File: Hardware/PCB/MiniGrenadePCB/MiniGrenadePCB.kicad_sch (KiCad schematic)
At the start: 3 parts, among them U1 DF-Player_mini, U2 WeMos_D1_mini

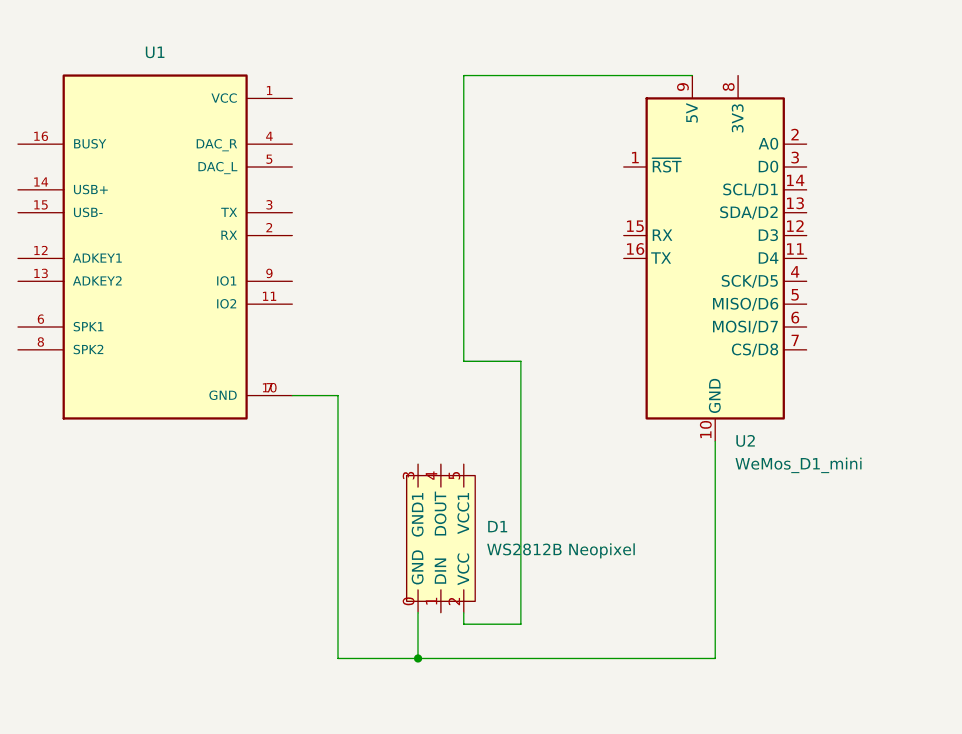
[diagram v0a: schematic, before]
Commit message: Corrected PCB Oopsie+ began small grenade PCB
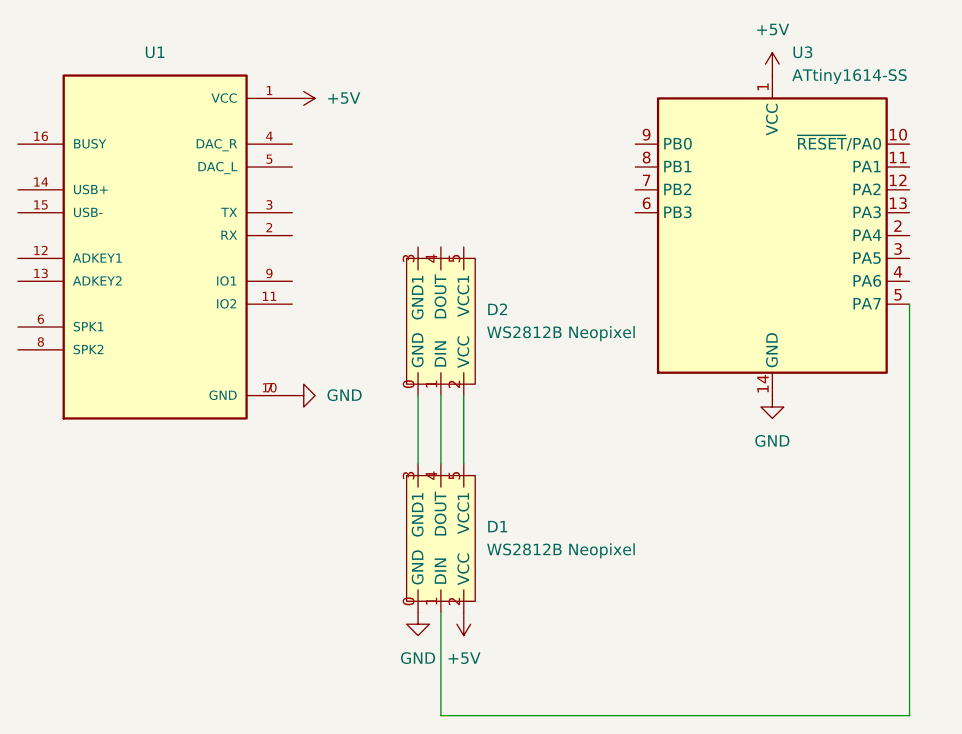
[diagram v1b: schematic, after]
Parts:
- removed U2: WeMos_D1_mini, Module:WEMOS_D1_mini_light, symbol MCU_Module:WeMos_D1_mini
- added D2: WS2812B Neopixel, Grenade_Stuff:NeoPixel_strip, symbol GrenadeStuff:NeoPixelStrip
- added U3: ATtiny1614-SS, Package_SO:SOIC-14_3.9x8.7mm_P1.27mm, symbol MCU_Microchip_ATtiny:ATtiny1614-SS
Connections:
- net GND: now reaches D1.0 (GND), U1.10 (GND), U1.7 (GND)
- net GND: now also U3.14 (GND)
- net at D1.1 (DIN): now also U3.5 (PA7)
- net +5V: now reaches D1.2 (VCC)
- net +5V: now also U1.1 (VCC), U3.1 (VCC)
- net at D1.3 (GND1): now also D2.0 (GND)
- net at D1.4 (DOUT): now also D2.1 (DIN)
- net at D1.5 (VCC1): now also D2.2 (VCC)
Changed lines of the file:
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@@
 (kicad_sch (version 20230121) (generator eeschema)
   (paper "A4")
-  (junction (at 165.1 138.43) (diameter 0) (color 0 0 0 0)
-  )
-  (wire (pts (xy 198.12 138.43) (xy 198.12 114.3))
-    (stroke (width 0) (type default))
-  )
-  (wire (pts (xy 170.18 73.66) (xy 170.18 105.41))
-    (stroke (width 0) (type default))
-  )
-  (wire (pts (xy 176.53 105.41) (xy 176.53 134.62))
-    (stroke (width 0) (type default))
-  )
-  (wire (pts (xy 170.18 105.41) (xy 176.53 105.41))
-    (stroke (width 0) (type default))
-  )
-  (wire (pts (xy 170.18 73.66) (xy 195.58 73.66))
-    (stroke (width 0) (type default))
-  )
-  (wire (pts (xy 165.1 138.43) (xy 165.1 133.35))
-    (stroke (width 0) (type default))
-  )
-  (wire (pts (xy 151.13 109.22) (xy 156.21 109.22))
-    (stroke (width 0) (type default))
-  )
-  (wire (pts (xy 170.18 134.62) (xy 170.18 133.35))
-    (stroke (width 0) (type default))
-  )
-  (wire (pts (xy 156.21 109.22) (xy 156.21 138.43))
-    (stroke (width 0) (type default))
-  )
-  (wire (pts (xy 165.1 138.43) (xy 198.12 138.43))
-    (stroke (width 0) (type default))
-  )
-  (wire (pts (xy 156.21 138.43) (xy 165.1 138.43))
-    (stroke (width 0) (type default))
-  )
-  (wire (pts (xy 176.53 134.62) (xy 170.18 134.62))
+  (wire (pts (xy 165.1 109.22) (xy 165.1 116.84))
+    (stroke (width 0) (type default))
+  )
+  (wire (pts (xy 170.18 109.22) (xy 170.18 116.84))
+    (stroke (width 0) (type default))
+  )
+  (wire (pts (xy 167.64 109.22) (xy 167.64 116.84))
+    (stroke (width 0) (type default))
+  )
+  (wire (pts (xy 167.64 133.35) (xy 167.64 144.78))
+    (stroke (width 0) (type default))
+  )
+  (wire (pts (xy 219.71 99.06) (xy 219.71 144.78))
+    (stroke (width 0) (type default))
+  )
+  (wire (pts (xy 167.64 144.78) (xy 219.71 144.78))
     (stroke (width 0) (type default))
   )
@@
     )
   )
-  (symbol (lib_id "MCU_Module:WeMos_D1_mini") (at 198.12 93.98 0) (unit 1)
-    (in_bom yes) (on_board yes) (dnp no) (fields_autoplaced)
-    (property "Reference" "U2" (at 200.3141 114.3 0)
-      (effects (font (size 1.27 1.27)) (justify left))
-    )
-    (property "Value" "WeMos_D1_mini" (at 200.3141 116.84 0)
-      (effects (font (size 1.27 1.27)) (justify left))
-    )
-    (property "Footprint" "Module:WEMOS_D1_mini_light" (at 198.12 123.19 0)
-      (effects (font (size 1.27 1.27)) hide)
-    )
-    (property "Datasheet" "https://wiki.wemos.cc/products:d1:d1_mini#documentation" (at 151.13 123.19 0)
-      (effects (font (size 1.27 1.27)) hide)
-    )
-    (pin "7")
-    (pin "13")
-    (pin "12")
-    (pin "11")
+  (symbol (lib_id "GrenadeStuff:NeoPixelStrip") (at 167.64 105.41 0) (unit 1)
+    (in_bom yes) (on_board yes) (dnp no) (fields_autoplaced)
+    (property "Reference" "D2" (at 172.72 99.695 0)
+      (effects (font (size 1.27 1.27)) (justify left))
+    )
+    (property "Value" "WS2812B Neopixel" (at 172.72 102.235 0)
+      (effects (font (size 1.27 1.27)) (justify left))
+    )
+    (property "Footprint" "Grenade_Stuff:NeoPixel_strip" (at 167.64 105.41 0)
+      (effects (font (size 1.27 1.27)) hide)
+    )
+    (property "Datasheet" "" (at 167.64 105.41 0)
+      (effects (font (size 1.27 1.27)) hide)
+    )
+    (pin "5")
+    (pin "2")
     (pin "4")
-    (pin "5")
-    (pin "14")
-    (pin "15")
-    (pin "6")
-    (pin "2")
     (pin "3")
-    (pin "1")
-    (pin "10")
-    (pin "16")
-    (pin "9")
-    (pin "8")
-    (instances
-      (project "MiniGrenadePCB"
-        (path "/903d1f49-37b0-45d7-9079-bf49af1c090a"
-          (reference "U2") (unit 1)
+    (pin "0")
+    (pin "1")
+    (instances
+      (project "MiniGrenadePCB"
+        (path "/903d1f49-37b0-45d7-9079-bf49af1c090a"
+          (reference "D2") (unit 1)
+        )
+      )
+    )
+  )
+  (symbol (lib_id "power:+5V") (at 170.18 133.35 180) (unit 1)
+    (in_bom yes) (on_board yes) (dnp no) (fields_autoplaced)
+    (property "Reference" "#PWR02" (at 170.18 129.54 0)
+      (effects (font (size 1.27 1.27)) hide)
+    )
+    (property "Value" "+5V" (at 170.18 138.43 0)
+      (effects (font (size 1.27 1.27)))
+    )
+    (property "Footprint" "" (at 170.18 133.35 0)
+      (effects (font (size 1.27 1.27)) hide)
+    )
+    (property "Datasheet" "" (at 170.18 133.35 0)
+      (effects (font (size 1.27 1.27)) hide)
+    )
+    (pin "1")
+    (instances
+      (project "MiniGrenadePCB"
+        (path "/903d1f49-37b0-45d7-9079-bf49af1c090a"
+          (reference "#PWR02") (unit 1)
+        )
+      )
+    )
+  )
+  (symbol (lib_id "power:+5V") (at 151.13 76.2 270) (unit 1)
+    (in_bom yes) (on_board yes) (dnp no) (fields_autoplaced)
+    (property "Reference" "#PWR04" (at 147.32 76.2 0)
+      (effects (font (size 1.27 1.27)) hide)
+    )
+    (property "Value" "+5V" (at 154.94 76.2 90)
+      (effects (font (size 1.27 1.27)) (justify left))
+    )
+    (property "Footprint" "" (at 151.13 76.2 0)
+      (effects (font (size 1.27 1.27)) hide)
+    )
+    (property "Datasheet" "" (at 151.13 76.2 0)
+      (effects (font (size 1.27 1.27)) hide)
+    )
+    (pin "1")
+    (instances
+      (project "MiniGrenadePCB"
+        (path "/903d1f49-37b0-45d7-9079-bf49af1c090a"
+          (reference "#PWR04") (unit 1)
+        )
+      )
+    )
+  )
+  (symbol (lib_id "power:GND") (at 151.13 109.22 90) (unit 1)
+    (in_bom yes) (on_board yes) (dnp no) (fields_autoplaced)
+    (property "Reference" "#PWR06" (at 157.48 109.22 0)
+      (effects (font (size 1.27 1.27)) hide)
+    )
+    (property "Value" "GND" (at 154.94 109.22 90)
+      (effects (font (size 1.27 1.27)) (justify right))
+    )
+    (property "Footprint" "" (at 151.13 109.22 0)
+      (effects (font (size 1.27 1.27)) hide)
+    )
+    (property "Datasheet" "" (at 151.13 109.22 0)
+      (effects (font (size 1.27 1.27)) hide)
+    )
+    (pin "1")
+    (instances
+      (project "MiniGrenadePCB"
+        (path "/903d1f49-37b0-45d7-9079-bf49af1c090a"
+          (reference "#PWR06") (unit 1)
+        )
+      )
+    )
+  )
+  (symbol (lib_id "power:GND") (at 204.47 109.22 0) (unit 1)
+    (in_bom yes) (on_board yes) (dnp no) (fields_autoplaced)
+    (property "Reference" "#PWR01" (at 204.47 115.57 0)
+      (effects (font (size 1.27 1.27)) hide)
+    )
+    (property "Value" "GND" (at 204.47 114.3 0)
+      (effects (font (size 1.27 1.27)))
+    )
+    (property "Footprint" "" (at 204.47 109.22 0)
+      (effects (font (size 1.27 1.27)) hide)
+    )
+    (property "Datasheet" "" (at 204.47 109.22 0)
+      (effects (font (size 1.27 1.27)) hide)
+    )
+    (pin "1")
+    (instances
+      (project "MiniGrenadePCB"
+        (path "/903d1f49-37b0-45d7-9079-bf49af1c090a"
+          (reference "#PWR01") (unit 1)
+        )
+      )
+    )
+  )
+  (symbol (lib_id "power:+5V") (at 204.47 73.66 0) (unit 1)
+    (in_bom yes) (on_board yes) (dnp no) (fields_autoplaced)
+    (property "Reference" "#PWR03" (at 204.47 77.47 0)
+      (effects (font (size 1.27 1.27)) hide)
+    )
+    (property "Value" "+5V" (at 204.47 68.58 0)
+      (effects (font (size 1.27 1.27)))
+    )
+    (property "Footprint" "" (at 204.47 73.66 0)
+      (effects (font (size 1.27 1.27)) hide)
+    )
+    (property "Datasheet" "" (at 204.47 73.66 0)
+      (effects (font (size 1.27 1.27)) hide)
+    )
+    (pin "1")
+    (instances
+      (project "MiniGrenadePCB"
+        (path "/903d1f49-37b0-45d7-9079-bf49af1c090a"
+          (reference "#PWR03") (unit 1)
         )
       )
@@
         )
       )
+    )
+  )
+  (symbol (lib_id "MCU_Microchip_ATtiny:ATtiny1614-SS") (at 204.47 91.44 0) (unit 1)
+    (in_bom yes) (on_board yes) (dnp no) (fields_autoplaced)
+    (property "Reference" "U3" (at 206.6641 71.12 0)
+      (effects (font (size 1.27 1.27)) (justify left))
+    )
+    (property "Value" "ATtiny1614-SS" (at 206.6641 73.66 0)
+      (effects (font (size 1.27 1.27)) (justify left))
+    )
+    (property "Footprint" "Package_SO:SOIC-14_3.9x8.7mm_P1.27mm" (at 204.47 91.44 0)
+      (effects (font (size 1.27 1.27) italic) hide)
+    )
+    (property "Datasheet" "http://ww1.microchip.com/downloads/en/DeviceDoc/ATtiny1614-data-sheet-40001995A.pdf" (at 204.47 91.44 0)
+      (effects (font (size 1.27 1.27)) hide)
+    )
+    (pin "4")
+    (pin "6")
+    (pin "5")
+    (pin "11")
+    (pin "1")
+    (pin "9")
+    (pin "7")
+    (pin "10")
+    (pin "2")
+    (pin "8")
+    (pin "14")
+    (pin "3")
+    (pin "13")
+    (pin "12")
+    (instances
+      (project "MiniGrenadePCB"
+        (path "/903d1f49-37b0-45d7-9079-bf49af1c090a"
+          (reference "U3") (unit 1)
+        )
+      )
+    )
+  )
+  (symbol (lib_id "power:GND") (at 165.1 133.35 0) (unit 1)
+    (in_bom yes) (on_board yes) (dnp no) (fields_autoplaced)
+    (property "Reference" "#PWR05" (at 165.1 139.7 0)
+      (effects (font (size 1.27 1.27)) hide)
+    )
+    (property "Value" "GND" (at 165.1 138.43 0)
+      (effects (font (size 1.27 1.27)))
+    )
+    (property "Footprint" "" (at 165.1 133.35 0)
+      (effects (font (size 1.27 1.27)) hide)
+    )
+    (property "Datasheet" "" (at 165.1 133.35 0)
+      (effects (font (size 1.27 1.27)) hide)
+    )
+    (pin "1")
+    (instances
+      (project "MiniGrenadePCB"
+        (path "/903d1f49-37b0-45d7-9079-bf49af1c090a"
+          (reference "#PWR05") (unit 1)
+        )
+      )
